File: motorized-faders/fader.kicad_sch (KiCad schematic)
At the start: 2 parts

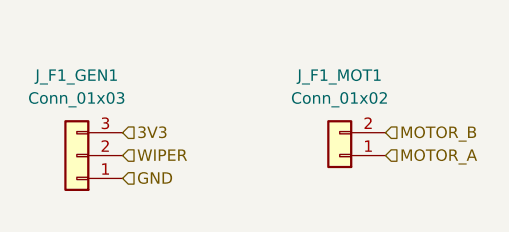
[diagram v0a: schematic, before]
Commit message: hw: single keyed JST-XH connector per fader and per display
Replace the per-fader 1x02 motor + 1x03 wiper/power headers with one
B5B-XH-A (MOTOR_A, MOTOR_B, GND, WIPER, 3V3) and move display headers to
B8B-XH-A in the same family. Keyed housings prevent reversed plugs
shorting 3.3 V to GND. PCB layout still needs Update from Schematic.

Co-Authored-By: Claude Opus 5.5 <noreply@anthropic.com>
Claude-Session: https://claude.ai/code/session_01KVW9PXPtP6oAbBUGi54MaJ
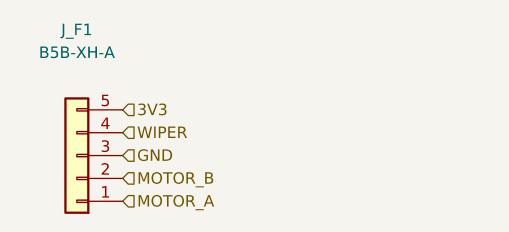
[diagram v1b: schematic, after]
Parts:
- removed J_F1_MOT1: Conn_01x02, Connector_PinHeader_2.54mm:PinHeader_1x02_P2.54mm_Vertical, symbol Connector_Generic:Conn_01x02
- J_F1: renamed from J_F1_GEN1; value Conn_01x03 -> B5B-XH-A; footprint Connector_PinHeader_2.54mm:PinHeader_1x03_P2.54mm_Vertical -> Connector_JST:JST_XH_B5B-XH-A_1x05_P2.50mm_Vertical; symbol Connector_Generic:Conn_01x03 -> Connector_Generic:Conn_01x05
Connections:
- net 3V3: now also J_F1.5 (Pin_5); no longer J_F1.3 (Pin_3)
- net GND: now also J_F1.3 (Pin_3); no longer J_F1.1 (Pin_1)
- net MOTOR_A: now also J_F1.1 (Pin_1)
- net MOTOR_B: now also J_F1.2 (Pin_2)
- net WIPER: now also J_F1.4 (Pin_4); no longer J_F1.2 (Pin_2)
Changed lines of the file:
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@@
 	(hierarchical_label "WIPER"
+		(shape input)
+		(at 160.02 55.88 0)
+		(effects
+			(font
+				(size 1.27 1.27)
+			)
+			(justify left)
+		)
+	)
+	(hierarchical_label "GND"
 		(shape input)
 		(at 160.02 58.42 0)
@@
 		)
 	)
-	(hierarchical_label "GND"
+	(hierarchical_label "MOTOR_A"
+		(shape input)
+		(at 160.02 63.5 0)
+		(effects
+			(font
+				(size 1.27 1.27)
+			)
+			(justify left)
+		)
+	)
+	(hierarchical_label "MOTOR_B"
 		(shape input)
 		(at 160.02 60.96 0)
@@
 		)
 	)
-	(hierarchical_label "MOTOR_A"
-		(shape input)
-		(at 189.23 58.42 0)
-		(effects
-			(font
-				(size 1.27 1.27)
-			)
-			(justify left)
-		)
-	)
-	(hierarchical_label "MOTOR_B"
-		(shape input)
-		(at 189.23 55.88 0)
-		(effects
-			(font
-				(size 1.27 1.27)
-			)
-			(justify left)
-		)
-	)
 	(hierarchical_label "3V3"
 		(shape input)
-		(at 160.02 55.88 0)
+		(at 160.02 53.34 0)
 		(effects
 			(font
@@
 	)
 	(symbol
-		(lib_id "Connector_Generic:Conn_01x02")
-		(at 184.15 58.42 180)
-		(unit 1)
-		(body_style 1)
-		(exclude_from_sim no)
-		(in_bom yes)
-		(on_board yes)
-		(in_pos_files yes)
-		(dnp no)
-		(fields_autoplaced yes)
-		(property "Reference" "J_F1_MOT1"
-			(at 184.15 49.53 0)
-			(show_name no)
-			(do_not_autoplace no)
-			(effects
-				(font
-					(size 1.27 1.27)
-				)
-			)
-		)
-		(property "Value" "Conn_01x02"
-			(at 184.15 52.07 0)
-			(show_name no)
-			(do_not_autoplace no)
-			(effects
-				(font
-					(size 1.27 1.27)
-				)
-			)
-		)
-		(property "Footprint" "Connector_PinHeader_2.54mm:PinHeader_1x02_P2.54mm_Vertical"
-			(at 184.15 58.42 0)
-			(hide yes)
-			(show_name no)
-			(do_not_autoplace no)
-			(effects
-				(font
-					(size 1.27 1.27)
-				)
-			)
-		)
-		(property "Datasheet" ""
-			(at 184.15 58.42 0)
-			(hide yes)
-			(show_name no)
-			(do_not_autoplace no)
-			(effects
-				(font
-					(size 1.27 1.27)
-				)
-			)
-		)
-		(property "Description" "Generic connector, single row, 01x02, script generated (kicad-library-utils/schlib/autogen/connector/)"
-			(at 184.15 58.42 0)
-			(hide yes)
-			(show_name no)
-			(do_not_autoplace no)
-			(effects
-				(font
-					(size 1.27 1.27)
-				)
-			)
-		)
-		(pin "2"
-		)
-		(pin "1"
-		)
-		(instances
-			(project "motorized-faders"
-				(path "/b7e3fc1e-7c8d-4632-8bd7-928f8e22b8b2/64389fec-fb00-4186-b5b1-261536e6c62d"
-					(reference "J_F3_MOT1")
-					(unit 1)
-				)
-				(path "/b7e3fc1e-7c8d-4632-8bd7-928f8e22b8b2/889cac32-bfc7-4106-895c-77c1ed4d1afb"
-					(reference "J_F2_MOT1")
-					(unit 1)
-				)
-				(path "/b7e3fc1e-7c8d-4632-8bd7-928f8e22b8b2/bac43807-ad40-4bbd-b72a-4b10a47f3691"
-					(reference "J_F4_MOT1")
-					(unit 1)
-				)
-				(path "/b7e3fc1e-7c8d-4632-8bd7-928f8e22b8b2/df0197ea-43aa-4e80-8ac6-816dff1fb039"
-					(reference "J_F1_MOT1")
-					(unit 1)
-				)
-			)
-		)
-	)
-	(symbol
-		(lib_id "Connector_Generic:Conn_01x03")
+		(lib_id "Connector_Generic:Conn_01x05")
 		(at 154.94 58.42 180)
 		(unit 1)
@@
 		(dnp no)
 		(fields_autoplaced yes)
-		(property "Reference" "J_F1_GEN1"
-			(at 154.94 49.53 0)
+		(property "Reference" "J_F1"
+			(at 154.94 44.45 0)
 			(show_name no)
 			(do_not_autoplace no)
@@
 			)
 		)
-		(property "Value" "Conn_01x03"
-			(at 154.94 52.07 0)
+		(property "Value" "B5B-XH-A"
+			(at 154.94 46.99 0)
 			(show_name no)
 			(do_not_autoplace no)
@@
 			)
 		)
-		(property "Footprint" "Connector_PinHeader_2.54mm:PinHeader_1x03_P2.54mm_Vertical"
+		(property "Footprint" "Connector_JST:JST_XH_B5B-XH-A_1x05_P2.50mm_Vertical"
 			(at 154.94 58.42 0)
 			(hide yes)
@@
 			)
 		)
-		(property "Description" "Generic connector, single row, 01x03, script generated (kicad-library-utils/schlib/autogen/connector/)"
+		(property "Description" "Generic connector, single row, 01x05, script generated (kicad-library-utils/schlib/autogen/connector/)"
 			(at 154.94 58.42 0)
 			(hide yes)
@@
 			)
 		)
-		(pin "3"
-		)
 		(pin "1"
 		)
 		(pin "2"
 		)
+		(pin "3"
+		)
+		(pin "4"
+		)
+		(pin "5"
+		)
 		(instances
 			(project "motorized-faders"
 				(path "/b7e3fc1e-7c8d-4632-8bd7-928f8e22b8b2/64389fec-fb00-4186-b5b1-261536e6c62d"
-					(reference "J_F3_GEN1")
+					(reference "J_F3")
 					(unit 1)
 				)
 				(path "/b7e3fc1e-7c8d-4632-8bd7-928f8e22b8b2/889cac32-bfc7-4106-895c-77c1ed4d1afb"
-					(reference "J_F2_GEN1")
+					(reference "J_F2")
 					(unit 1)
 				)
 				(path "/b7e3fc1e-7c8d-4632-8bd7-928f8e22b8b2/bac43807-ad40-4bbd-b72a-4b10a47f3691"
-					(reference "J_F4_GEN1")
+					(reference "J_F4")
 					(unit 1)
 				)
 				(path "/b7e3fc1e-7c8d-4632-8bd7-928f8e22b8b2/df0197ea-43aa-4e80-8ac6-816dff1fb039"
-					(reference "J_F1_GEN1")
+					(reference "J_F1")
 					(unit 1)
 				)
